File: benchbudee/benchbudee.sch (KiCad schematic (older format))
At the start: 0 parts

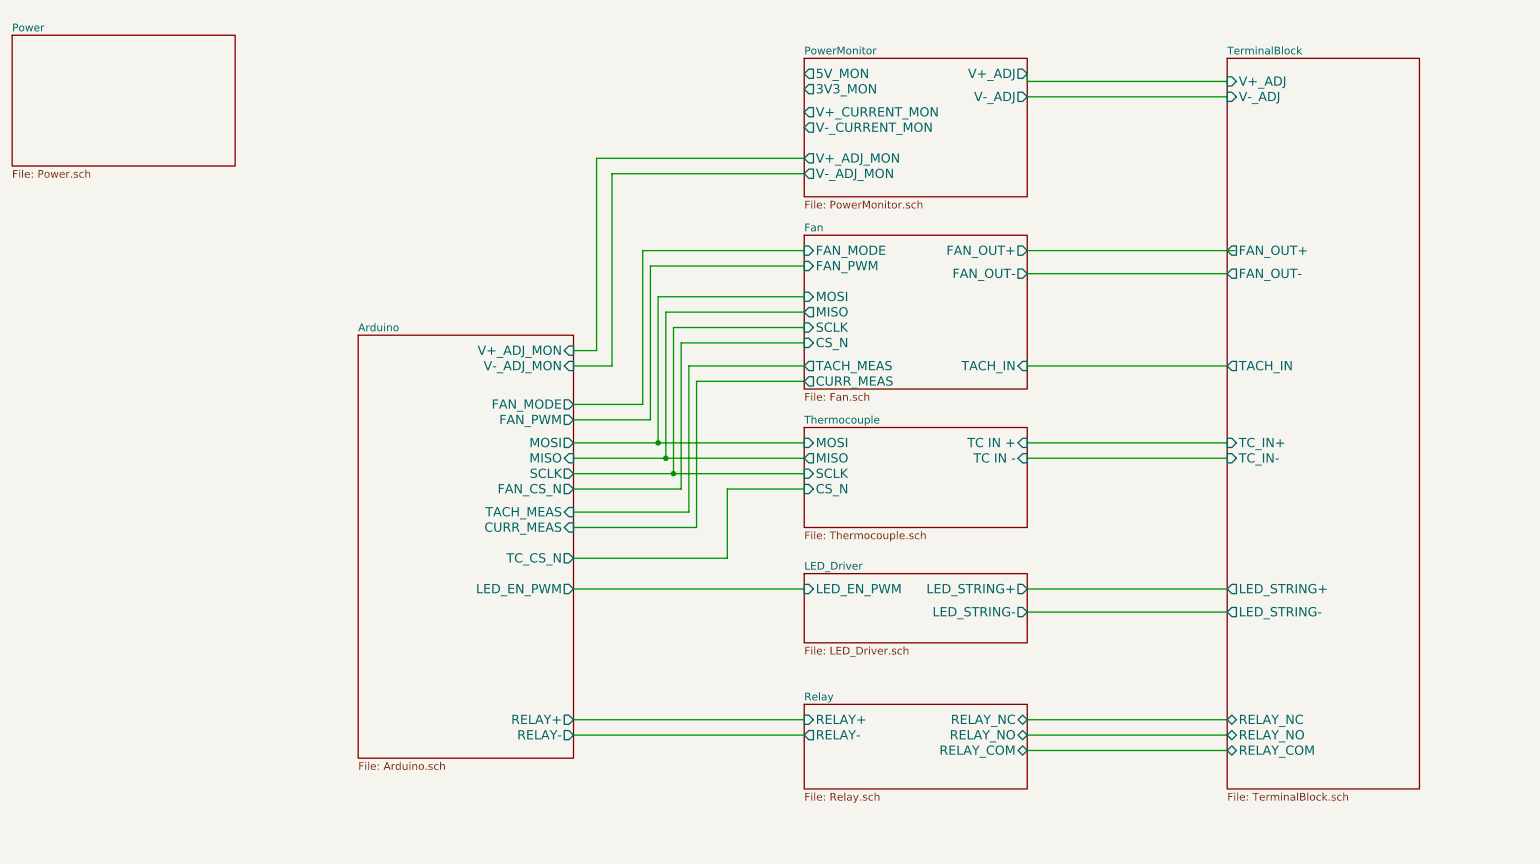
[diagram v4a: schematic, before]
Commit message: Schematic and associations for the thermocouple module
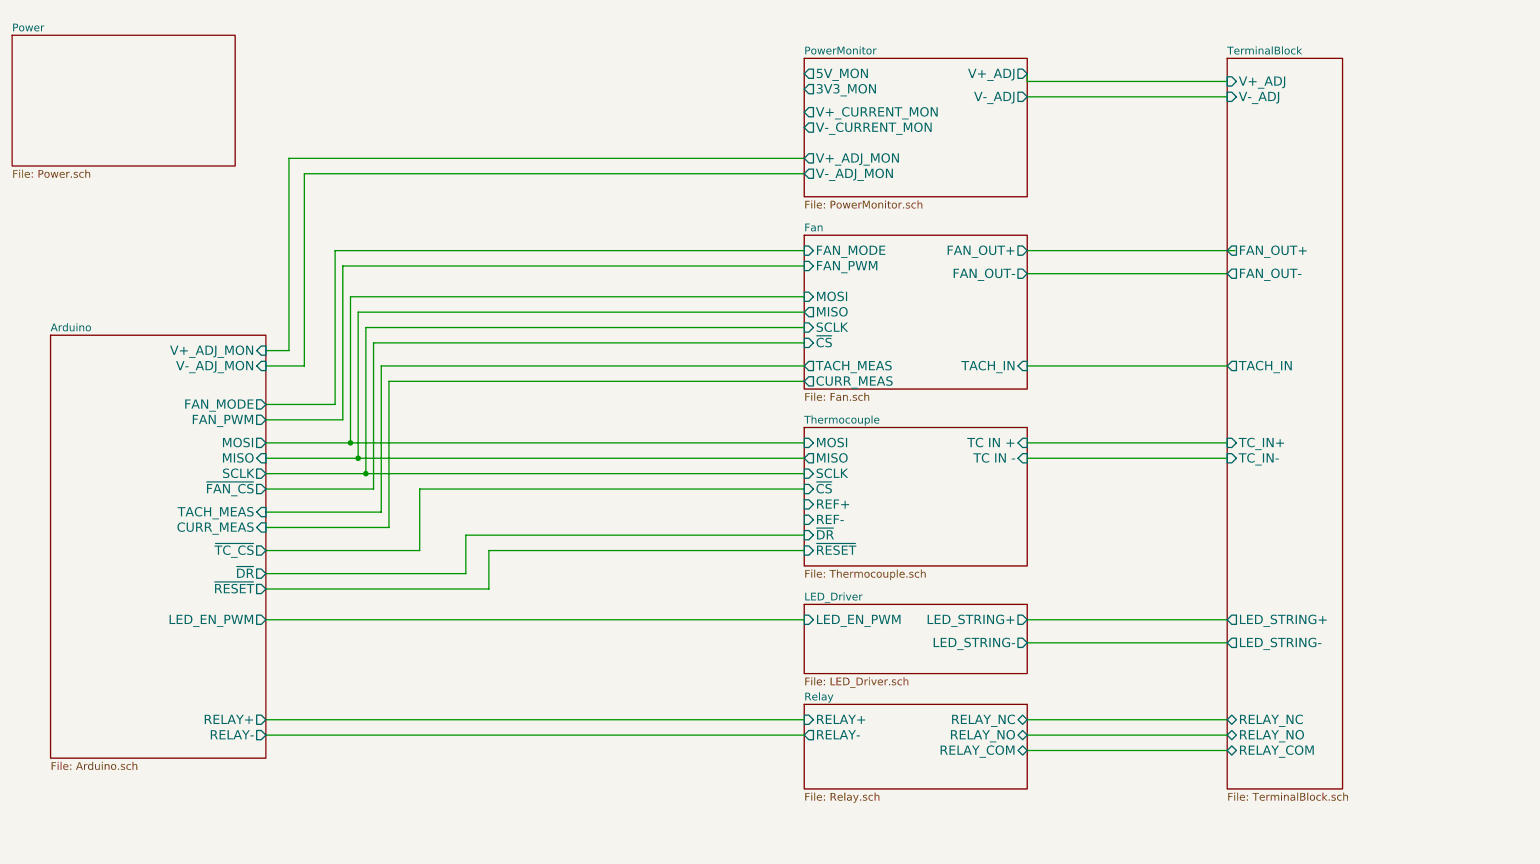
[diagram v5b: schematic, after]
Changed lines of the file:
@@
 $EndDescr
 $Sheet
-S 6250 3500 1450 650
+S 6250 3500 1450 900
 U 52F13E8B
 F0 "Thermocouple" 50
@@
 F5 "MISO" O L 6250 3700 60
 F6 "SCLK" I L 6250 3800 60
-F7 "CS_N" I L 6250 3900 60
+F7 "~CS" I L 6250 3900 60
+F8 "REF+" I L 6250 4000 60
+F9 "REF-" I L 6250 4100 60
+F10 "~DR" I L 6250 4200 60
+F11 "~RESET" I L 6250 4300 60
 $EndSheet
 $Sheet
@@
 $EndSheet
 $Sheet
-S 6250 4450 1450 450
+S 6250 4650 1450 450
 U 52F1408A
 F0 "LED_Driver" 50
 F1 "LED_Driver.sch" 50
-F2 "LED_EN_PWM" I L 6250 4550 60
-F3 "LED_STRING+" O R 7700 4550 60
-F4 "LED_STRING-" O R 7700 4700 60
+F2 "LED_EN_PWM" I L 6250 4750 60
+F3 "LED_STRING+" O R 7700 4750 60
+F4 "LED_STRING-" O R 7700 4900 60
 $EndSheet
 $Sheet
@@
 	7700 5600 9000 5600
 Wire Wire Line
-	4750 3000 4900 3000
-Wire Wire Line
-	4900 3000 4900 1750
-Wire Wire Line
-	4900 1750 6250 1750
-Wire Wire Line
-	4750 3100 5000 3100
-Wire Wire Line
-	5000 3100 5000 1850
-Wire Wire Line
-	5000 1850 6250 1850
-Wire Wire Line
-	4750 3450 5250 3450
-Wire Wire Line
-	5250 3450 5250 2450
-Wire Wire Line
-	5250 2450 6250 2450
-Wire Wire Line
-	4750 3600 6250 3600
-Wire Wire Line
-	5300 3600 5300 2650
-Wire Wire Line
-	5300 2650 6250 2650
-Wire Wire Line
-	4750 3700 6250 3700
-Wire Wire Line
-	5350 3700 5350 2750
-Wire Wire Line
-	5350 2750 6250 2750
-Wire Wire Line
-	5400 3800 5400 2850
-Wire Wire Line
-	5400 2850 6250 2850
-Wire Wire Line
-	4750 4050 5500 4050
-Wire Wire Line
-	5500 4050 5500 3100
-Wire Wire Line
-	5500 3100 6250 3100
-Wire Wire Line
-	4750 4150 5550 4150
-Wire Wire Line
-	5550 4150 5550 3200
-Wire Wire Line
-	5550 3200 6250 3200
-Wire Wire Line
-	4750 4550 6250 4550
-$Sheet
-S 9000 1100 1250 4750
+	2750 3000 2900 3000
+Wire Wire Line
+	2900 3000 2900 1750
+Wire Wire Line
+	2900 1750 6250 1750
+Wire Wire Line
+	2750 3100 3000 3100
+Wire Wire Line
+	3000 3100 3000 1850
+Wire Wire Line
+	3000 1850 6250 1850
+Wire Wire Line
+	2750 3450 3250 3450
+Wire Wire Line
+	3250 3450 3250 2450
+Wire Wire Line
+	3250 2450 6250 2450
+Wire Wire Line
+	2750 3600 6250 3600
+Wire Wire Line
+	3300 3600 3300 2650
+Wire Wire Line
+	3300 2650 6250 2650
+Wire Wire Line
+	2750 3700 6250 3700
+Wire Wire Line
+	3350 3700 3350 2750
+Wire Wire Line
+	3350 2750 6250 2750
+Wire Wire Line
+	3400 3800 3400 2850
+Wire Wire Line
+	3400 2850 6250 2850
+Wire Wire Line
+	2750 4050 3500 4050
+Wire Wire Line
+	3500 4050 3500 3100
+Wire Wire Line
+	3500 3100 6250 3100
+Wire Wire Line
+	2750 4150 3550 4150
+Wire Wire Line
+	3550 4150 3550 3200
+Wire Wire Line
+	3550 3200 6250 3200
+Wire Wire Line
+	2750 4750 6250 4750
+$Sheet
+S 9000 1100 750  4750
 U 52F140D2
 F0 "TerminalBlock" 50
@@
 F5 "FAN_OUT-" O L 9000 2500 60
 F6 "TACH_IN" O L 9000 3100 60
-F7 "LED_STRING+" O L 9000 4550 60
-F8 "LED_STRING-" O L 9000 4700 60
+F7 "LED_STRING+" O L 9000 4750 60
+F8 "LED_STRING-" O L 9000 4900 60
 F9 "TC_IN+" I L 9000 3600 60
 F10 "TC_IN-" I L 9000 3700 60
@@
 	7700 3700 9000 3700
 Wire Wire Line
-	7700 4550 9000 4550
-Wire Wire Line
-	7700 4700 9000 4700
-Connection ~ 5300 3600
-Connection ~ 5350 3700
-Wire Wire Line
-	4750 3800 6250 3800
-Connection ~ 5400 3800
-Wire Wire Line
-	4750 3900 5450 3900
-Wire Wire Line
-	5450 3900 5450 2950
-Wire Wire Line
-	5450 2950 6250 2950
-Wire Wire Line
-	4750 4350 5750 4350
-Wire Wire Line
-	5750 4350 5750 3900
-Wire Wire Line
-	5750 3900 6250 3900
-Wire Wire Line
-	4750 5400 6250 5400
-Wire Wire Line
-	6250 5500 4750 5500
-Wire Wire Line
-	4750 3350 5200 3350
-Wire Wire Line
-	5200 3350 5200 2350
-Wire Wire Line
-	5200 2350 6250 2350
+	7700 4900 9000 4900
+Wire Wire Line
+	7700 4750 9000 4750
+Connection ~ 3300 3600
+Connection ~ 3350 3700
+Wire Wire Line
+	2750 3800 6250 3800
+Connection ~ 3400 3800
+Wire Wire Line
+	2750 3900 3450 3900
+Wire Wire Line
+	3450 3900 3450 2950
+Wire Wire Line
+	3450 2950 6250 2950
+Wire Wire Line
+	2750 4300 3750 4300
+Wire Wire Line
+	3750 4300 3750 3900
+Wire Wire Line
+	3750 3900 6250 3900
+Wire Wire Line
+	2750 5400 6250 5400
+Wire Wire Line
+	6250 5500 2750 5500
+Wire Wire Line
+	2750 3350 3200 3350
+Wire Wire Line
+	3200 3350 3200 2350
+Wire Wire Line
+	3200 2350 6250 2350
 $Sheet
 S 6250 2250 1450 1000
@@
 F2 "MOSI" I L 6250 2650 60
 F3 "MISO" O L 6250 2750 60
-F4 "CS_N" I L 6250 2950 60
+F4 "~CS" I L 6250 2950 60
 F5 "SCLK" I L 6250 2850 60
 F6 "FAN_OUT+" O R 7700 2350 60
@@
 $EndSheet
 $Sheet
-S 3350 2900 1400 2750
+S 1350 2900 1400 2750
 U 52F13E2E
 F0 "Arduino" 50
 F1 "Arduino.sch" 50
-F2 "MOSI" O R 4750 3600 60
-F3 "MISO" I R 4750 3700 60
-F4 "SCLK" O R 4750 3800 60
-F5 "RELAY-" O R 4750 5500 60
-F6 "RELAY+" O R 4750 5400 60
-F7 "TACH_MEAS" I R 4750 4050 60
-F8 "CURR_MEAS" I R 4750 4150 60
-F9 "V+_ADJ_MON" I R 4750 3000 60
-F10 "V-_ADJ_MON" I R 4750 3100 60
-F11 "LED_EN_PWM" O R 4750 4550 60
-F12 "FAN_CS_N" O R 4750 3900 60
-F13 "TC_CS_N" O R 4750 4350 60
-F14 "FAN_PWM" O R 4750 3450 60
-F15 "FAN_MODE" O R 4750 3350 60
-$EndSheet
+F2 "MOSI" O R 2750 3600 60
+F3 "MISO" I R 2750 3700 60
+F4 "SCLK" O R 2750 3800 60
+F5 "RELAY-" O R 2750 5500 60
+F6 "RELAY+" O R 2750 5400 60
+F7 "TACH_MEAS" I R 2750 4050 60
+F8 "CURR_MEAS" I R 2750 4150 60
+F9 "V+_ADJ_MON" I R 2750 3000 60
+F10 "V-_ADJ_MON" I R 2750 3100 60
+F11 "LED_EN_PWM" O R 2750 4750 60
+F12 "~FAN_CS" O R 2750 3900 60
+F13 "~TC_CS" O R 2750 4300 60
+F14 "FAN_PWM" O R 2750 3450 60
+F15 "FAN_MODE" O R 2750 3350 60
+F16 "~RESET" O R 2750 4550 60
+F17 "~DR" O R 2750 4450 60
+$EndSheet
+Wire Wire Line
+	2750 4450 4050 4450
+Wire Wire Line
+	4050 4450 4050 4200
+Wire Wire Line
+	4050 4200 6250 4200
+Wire Wire Line
+	2750 4550 4200 4550
+Wire Wire Line
+	4200 4550 4200 4300
+Wire Wire Line
+	4200 4300 6250 4300
 $EndSCHEMATC
